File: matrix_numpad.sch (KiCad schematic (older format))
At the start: 55 parts, among them SW1 Rotary_Encoder_Switch, U1 MCP23017_SS, U2 IS31FL3731-SA

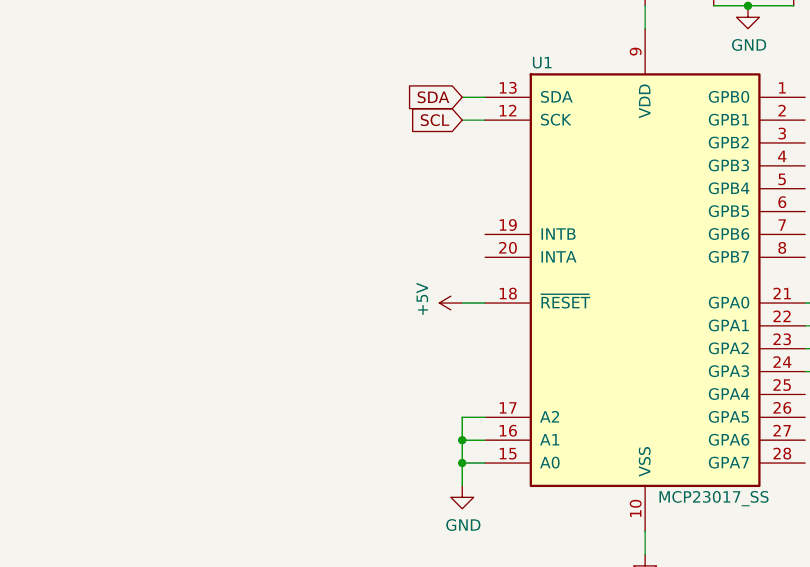
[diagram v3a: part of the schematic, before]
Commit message: Fix unconnected IO expander reset
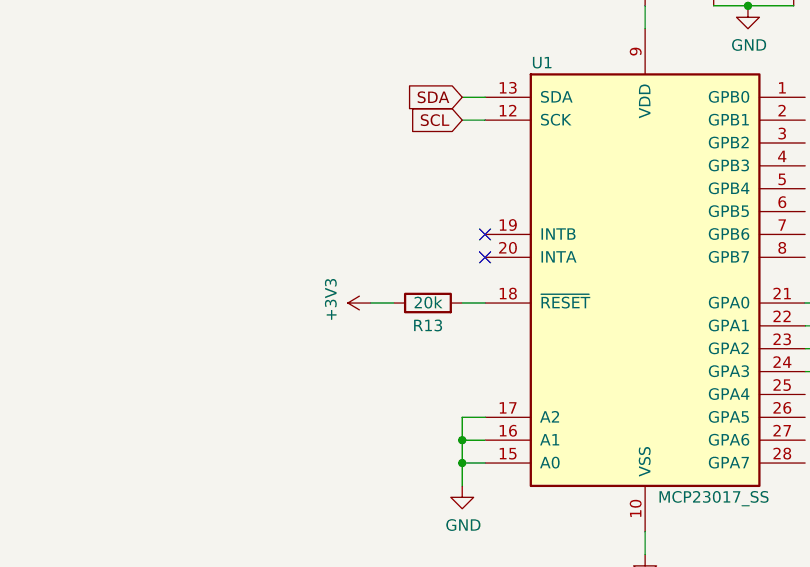
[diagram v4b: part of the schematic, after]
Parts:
- added R13: 20k, Resistor_SMD:R_0805_2012Metric_Pad1.15x1.40mm_HandSolder, symbol Device:R
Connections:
- net +3V3: now also R13.1
- net +5V: no longer names the net of U1.18 (~RESET~)
- net +5V: now also R13.2
- no-connect marks 16 -> 18
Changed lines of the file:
@@
 Wire Wire Line
 	10400 5200 10500 5200
-$Comp
-L power:+5V #PWR?
-U 1 1 5FFB2AC6
-P 10400 6000
-AR Path="/5FF53271/5FFB2AC6" Ref="#PWR?"  Part="1"
-AR Path="/5FF53271/5FF7CBCC/5FFB2AC6" Ref="#PWR?"  Part="1"
-AR Path="/5FF5604D/5FF9299E/5FFB2AC6" Ref="#PWR?"  Part="1"
-AR Path="/5FF77C9D/5FFB2AC6" Ref="#PWR?"  Part="1"
-AR Path="/5FF5604D/5FFB2AC6" Ref="#PWR0104"  Part="1"
-F 0 "#PWR0104" H 10400 5850 50  0001 C CNN
-F 1 "+5V" H 10415 6173 50  0000 C CNN
-F 2 "" H 10400 6000 50  0001 C CNN
-F 3 "" H 10400 6000 50  0001 C CNN
-	1    10400 6000
-	0    -1   -1   0
-$EndComp
 Wire Wire Line
 	10500 6000 10400 6000
@@
 Connection ~ 4300 5000
 $Comp
-L power:+3V3 #PWR?
+L power:+3V3 #PWR03
 U 1 1 604FDB56
 P 14450 5500
-F 0 "#PWR?" H 14450 5350 50  0001 C CNN
+F 0 "#PWR03" H 14450 5350 50  0001 C CNN
 F 1 "+3V3" H 14465 5673 50  0000 C CNN
 F 2 "" H 14450 5500 50  0001 C CNN
@@
 	0    -1   -1   0
 $EndComp
+$Comp
+L Device:R R13
+U 1 1 612EBB22
+P 10250 6000
+F 0 "R13" V 10150 6000 50  0000 C CNN
+F 1 "20k" V 10250 6000 50  0000 C CNN
+F 2 "Resistor_SMD:R_0805_2012Metric_Pad1.15x1.40mm_HandSolder" V 10180 6000 50  0001 C CNN
+F 3 "~" H 10250 6000 50  0001 C CNN
+	1    10250 6000
+	0    -1   -1   0
+$EndComp
+$Comp
+L power:+3V3 #PWR01
+U 1 1 612EC1C6
+P 10000 6000
+F 0 "#PWR01" H 10000 5850 50  0001 C CNN
+F 1 "+3V3" H 10015 6173 50  0000 C CNN
+F 2 "" H 10000 6000 50  0001 C CNN
+F 3 "" H 10000 6000 50  0001 C CNN
+	1    10000 6000
+	0    -1   -1   0
+$EndComp
+Wire Wire Line
+	10000 6000 10100 6000
+NoConn ~ 10500 5700
+NoConn ~ 10500 5800
 $EndSCHEMATC
